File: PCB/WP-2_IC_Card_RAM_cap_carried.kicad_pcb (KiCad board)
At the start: 2 copper layers, 14.5 x 48.5 mm, 10 parts, among them J1 Conn_01x38_Female, U1 SRAM 128Kx8 5v Parallel, U2 SRAM 128Kx8 5v Parallel

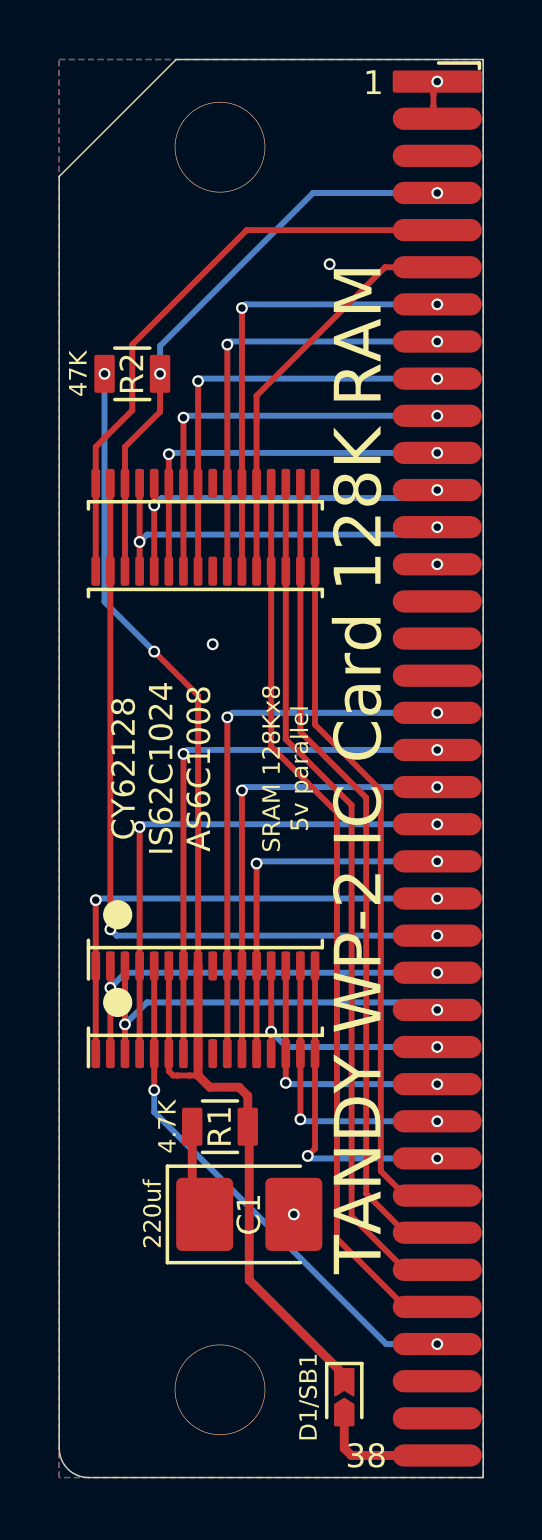
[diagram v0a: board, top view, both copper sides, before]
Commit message: fine-tune via-near-trace placements
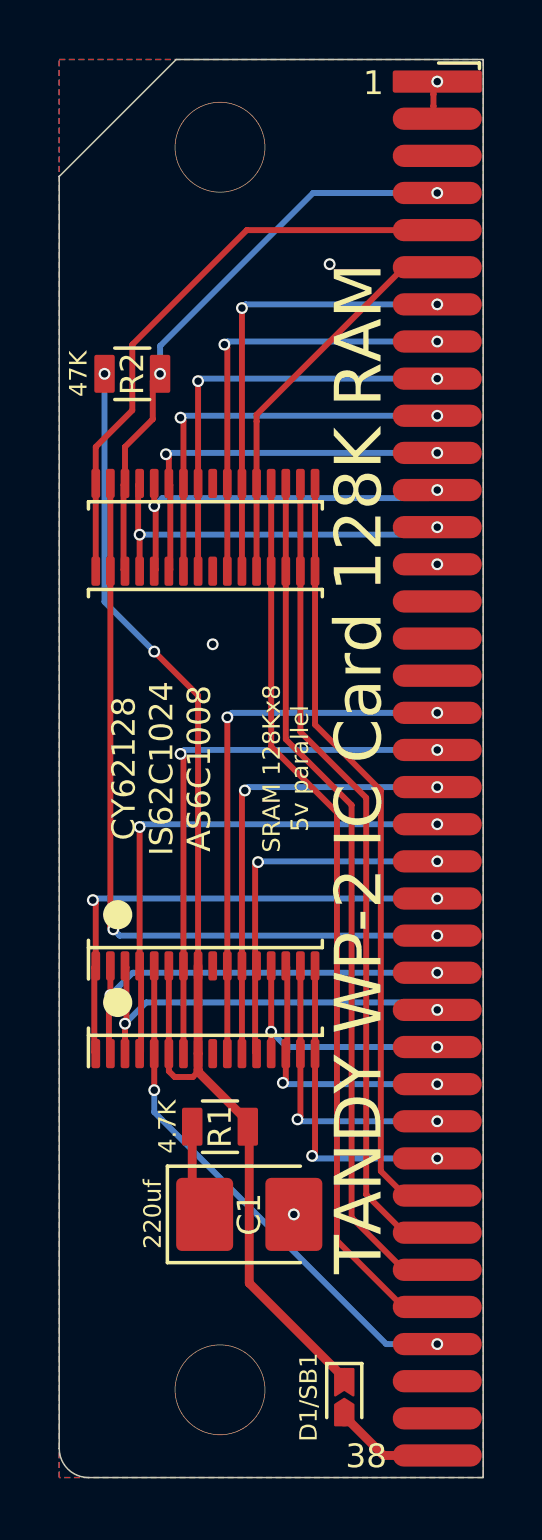
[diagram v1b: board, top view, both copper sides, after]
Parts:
- moved NT2 0.05 mm to (148.5, 110.2)
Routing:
- net VBUS: track 4.33 -> 3.72 mm

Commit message: increase via sizes and min soldermask width for PCBWAY
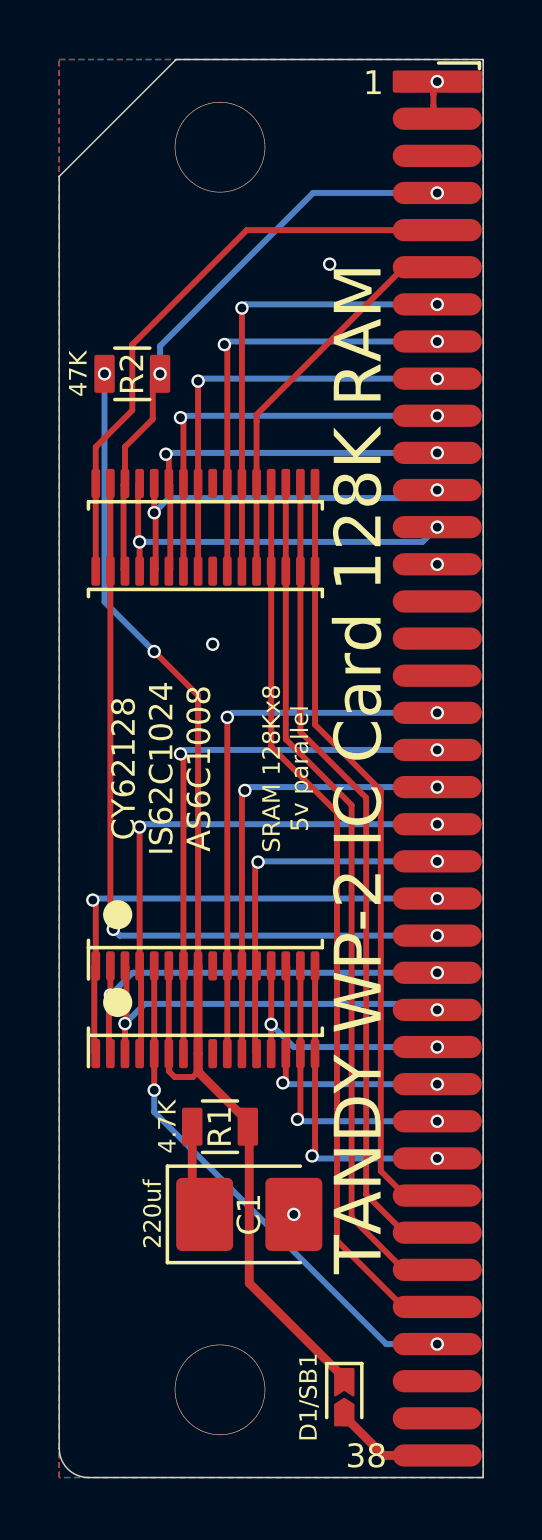
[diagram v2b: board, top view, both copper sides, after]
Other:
- net class Default: trace_width 0.254 -> 0.18; via_dia 0.4064 -> 0.46; via_drill 0.254 -> 0.3
- rule via_min_drill: 0.254 -> 0.3
- rule via_min_size: 0.4064 -> 0.46
